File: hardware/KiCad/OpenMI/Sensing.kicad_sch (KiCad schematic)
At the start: 11 parts, among them U2 INA381A2IDGS

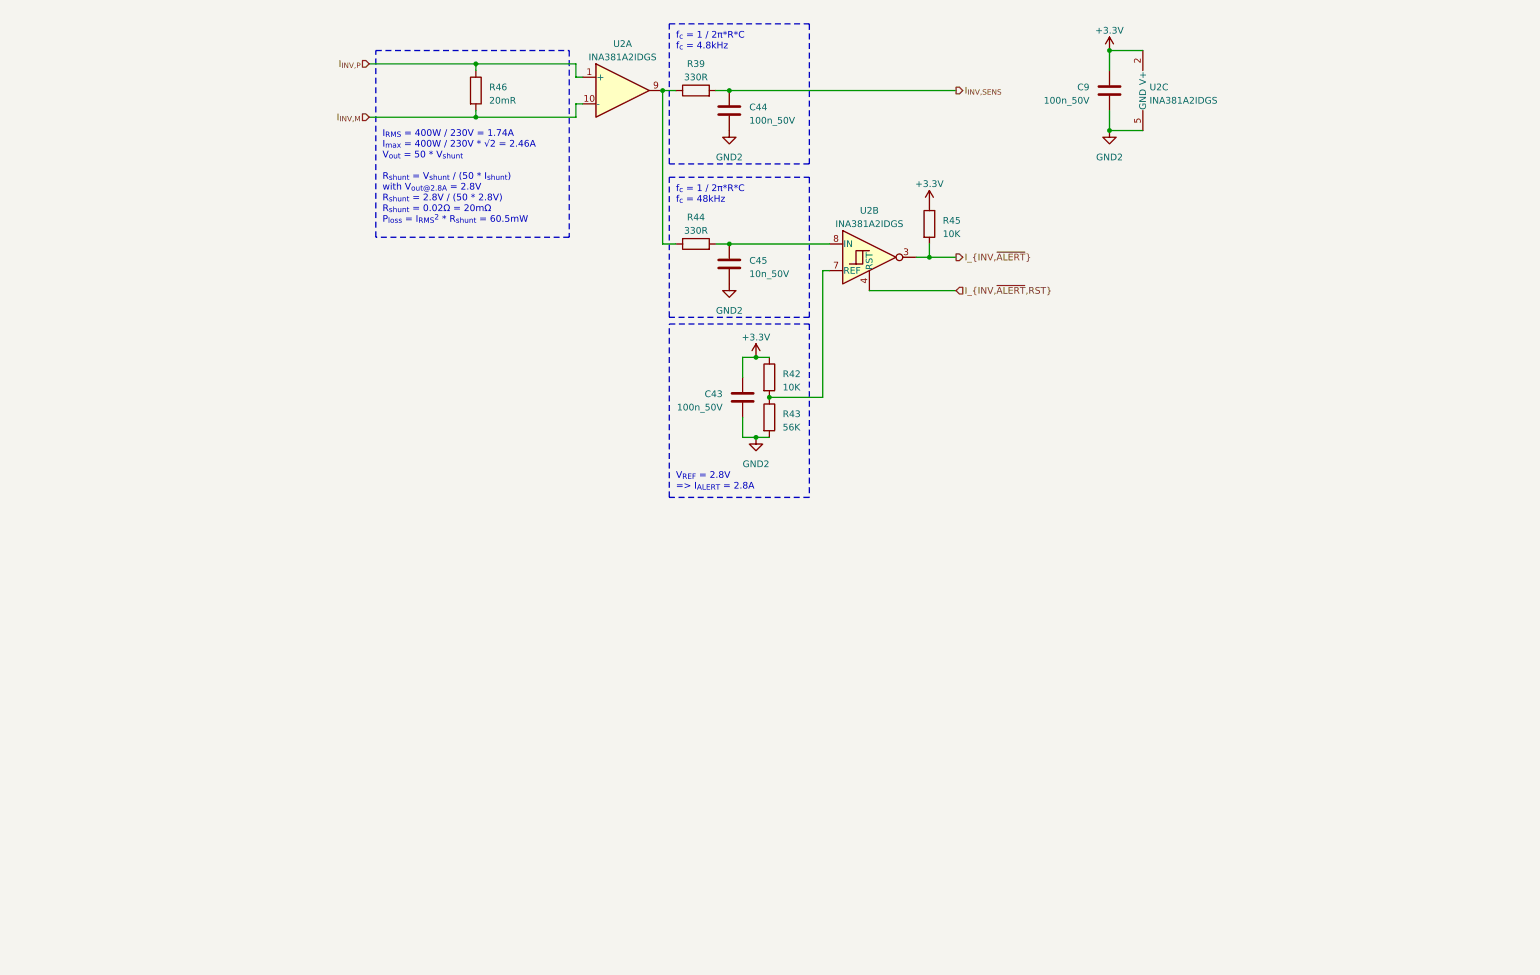
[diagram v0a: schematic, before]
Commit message: feat(hw): Moves DC-bus sense to Sensing sheet. Adds op-amp for impedance decoupling.
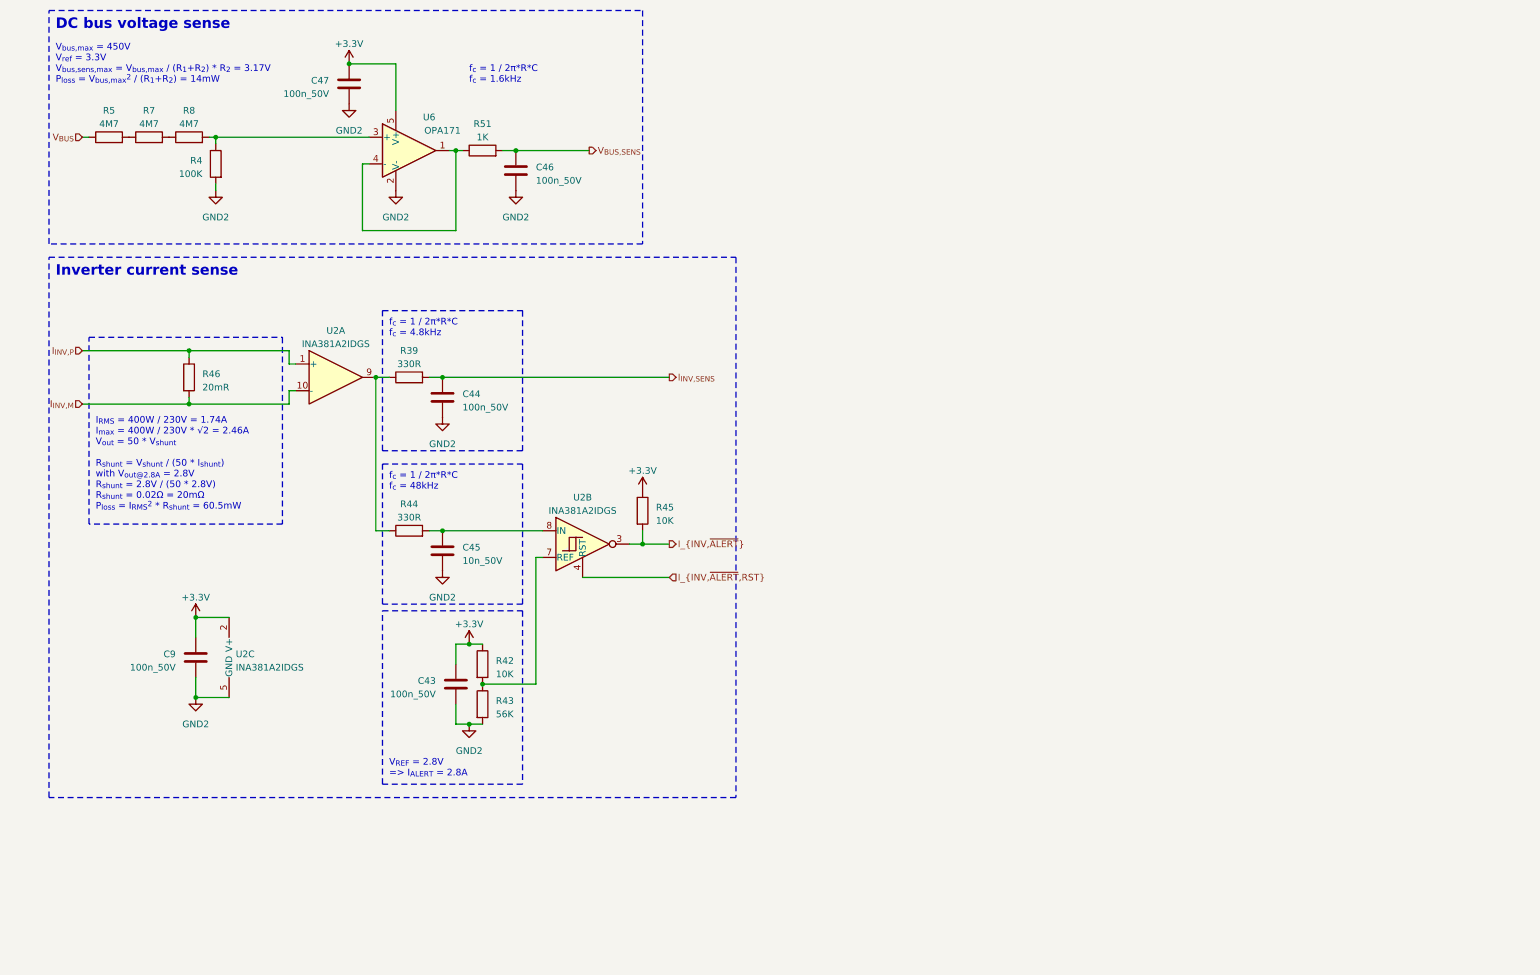
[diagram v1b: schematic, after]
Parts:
- added C46, C47: 100n_50V, Capacitor_SMD:C_0603_1608Metric, symbol _C_0603:100n_50V
- added R4: 100K, Resistor_SMD:R_0603_1608Metric, symbol _R_0603:100K
- added R5, R7, R8: 4M7, Resistor_SMD:R_1206_3216Metric, symbol _R_1206:4M7
- added R51: 1K, Resistor_SMD:R_0603_1608Metric, symbol _R_0603:1K
- added U6: OPA171, Package_TO_SOT_SMD:SOT-23-5, symbol _Amplifier_Operational:OPA171
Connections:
- net +3.3V: now also C47.1, U6.5 (V+)
- net GND2: now also C46.2, C47.2, R4.2, U6.2 (V-)
- new net: R7.2, R8.1
- new net: R4.1, R8.2, U6.3 (+)
- new net: R5.2, R7.1
- new net: R51.1, U6.1, U6.4 (-)
- new net V_{BUS,SENS}: C46.1, R51.2
- new net V_{BUS}: R5.1
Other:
- note added: "DC bus voltage sense"
- note added: "Inverter current sense"
- note added: "V_{bus,max} = 450V V_{ref} = 3.3V V_{bus,sens,max} = V_{bus,max} / (R_{1}+R_{2}) * R_{2} = 3.17V P_{loss} = V_{bus,max}^{2} / (R_{1}+R_{2}) = 14mW"
- note added: "f_{c} = 1 / 2π*R*C f_{c} = 1.6kHz"
- moved on the sheet: C43, C44, C45, C9, R39, R42, R43, R44, R45, R46, U2A, U2B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

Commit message: refactor(hw): Replaces OPA171 with pin compatible MCP6001T
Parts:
- removed U6: OPA171, Package_TO_SOT_SMD:SOT-23-5, symbol _Amplifier_Operational:OPA171
- added U7: MCP6001T-OT, Package_TO_SOT_SMD:SOT-23-5, symbol _Amplifier_Operational:MCP6001T-OT
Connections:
- net +3.3V: now also U7.5 (V+)
- net GND2: now also U7.2 (V-)
- net at R4.1, R8.2: now also U7.3 (+)
- net at R51.1: now also U7.1, U7.4 (-)
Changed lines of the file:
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@@
-    )
-  )
-  (symbol (lib_id "_Amplifier_Operational:OPA171") (at 82.55 40.64 0) (unit 1)
-    (in_bom yes) (on_board yes) (dnp no)
-    (property "Reference" "U6" (at 86.36 34.29 0)
-      (effects (font (size 1.27 1.27)))
-    )
-    (property "Value" "OPA171" (at 88.9 36.83 0)
-      (effects (font (size 1.27 1.27)))
-    )
-    (property "Footprint" "Package_TO_SOT_SMD:SOT-23-5" (at 82.55 40.64 0)
-      (effects (font (size 1.27 1.27)) hide)
-    )
-    (property "Datasheet" "http://www.ti.com/lit/ds/symlink/opa171.pdf" (at 82.55 35.56 0)
-      (effects (font (size 1.27 1.27)) hide)
-    )
-    (property "MF" "Texas Instruments" (at 82.55 40.64 0)
-      (effects (font (size 1.27 1.27)) hide)
-    )
-    (property "MPN" "OPA171AIDBV(R/T)" (at 82.55 40.64 0)
-      (effects (font (size 1.27 1.27)) hide)
-    )
-    (property "OC_CONRAD" "" (at 82.55 40.64 0)
-      (effects (font (size 1.27 1.27)) hide)
-    )
-    (property "OC_FARNELL" "" (at 82.55 40.64 0)
-      (effects (font (size 1.27 1.27)) hide)
-    )
-    (property "OC_LCSC" "" (at 82.55 40.64 0)
-      (effects (font (size 1.27 1.27)) hide)
-    )
-    (property "OC_MOUSER" "595-OPA171AIDBVR" (at 82.55 40.64 0)
-      (effects (font (size 1.27 1.27)) hide)
-    )
-    (property "OC_REICHELT" "" (at 82.55 40.64 0)
-      (effects (font (size 1.27 1.27)) hide)
-    )
-    (pin "2")
-    (pin "5")
-    (pin "1")
-    (pin "3")
-    (pin "4")
-    (instances
-      (project "OpenMI"
-        (path "/2d959e19-1572-42a0-a8fd-da8463ad4e66/bb3056b4-4e5d-4f2d-baa2-a568d9d3e754"
-          (reference "U6") (unit 1)
-        )
-      )
     )
   )
@@
         )
       )
+    )
+  )
+  (symbol (lib_id "_Amplifier_Operational:MCP6001T-OT") (at 82.55 40.64 0) (unit 1)
+    (in_bom yes) (on_board yes) (dnp no)
+    (property "Reference" "U7" (at 87.63 31.75 0)
+      (effects (font (size 1.27 1.27)))
+    )
+    (property "Value" "MCP6001T-OT" (at 87.63 34.29 0)
+      (effects (font (size 1.27 1.27)))
+    )
+    (property "Footprint" "Package_TO_SOT_SMD:SOT-23-5" (at 80.01 45.72 0)
+      (effects (font (size 1.27 1.27)) (justify left) hide)
+    )
+    (property "Datasheet" "http://ww1.microchip.com/downloads/en/DeviceDoc/MCP6001-1R-1U-2-4-1-MHz-Low-Power-Op-Amp-DS20001733L.pdf" (at 82.55 40.64 0)
+      (effects (font (size 1.27 1.27)) hide)
+    )
+    (property "MF" "Microchip Technology" (at 82.55 40.64 0)
+      (effects (font (size 1.27 1.27)) hide)
+    )
+    (property "MPN" "MCP6001T-I/OT" (at 82.55 40.64 0)
+      (effects (font (size 1.27 1.27)) hide)
+    )
+    (property "OC_CONRAD" "" (at 82.55 40.64 0)
+      (effects (font (size 1.27 1.27)) hide)
+    )
+    (property "OC_FARNELL" "" (at 82.55 40.64 0)
+      (effects (font (size 1.27 1.27)) hide)
+    )
+    (property "OC_LCSC" "C116490" (at 82.55 40.64 0)
+      (effects (font (size 1.27 1.27)) hide)
+    )
+    (property "OC_MOUSER" "579-MCP6001T-I/OT" (at 82.55 40.64 0)
+      (effects (font (size 1.27 1.27)) hide)
+    )
+    (property "OC_REICHELT" "" (at 82.55 40.64 0)
+      (effects (font (size 1.27 1.27)) hide)
+    )
+    (pin "2")
+    (pin "5")
+    (pin "1")
+    (pin "3")
+    (pin "4")
+    (instances
+      (project "OpenMI"
+        (path "/2d959e19-1572-42a0-a8fd-da8463ad4e66/bb3056b4-4e5d-4f2d-baa2-a568d9d3e754"
+          (reference "U7") (unit 1)
+        )
+      )

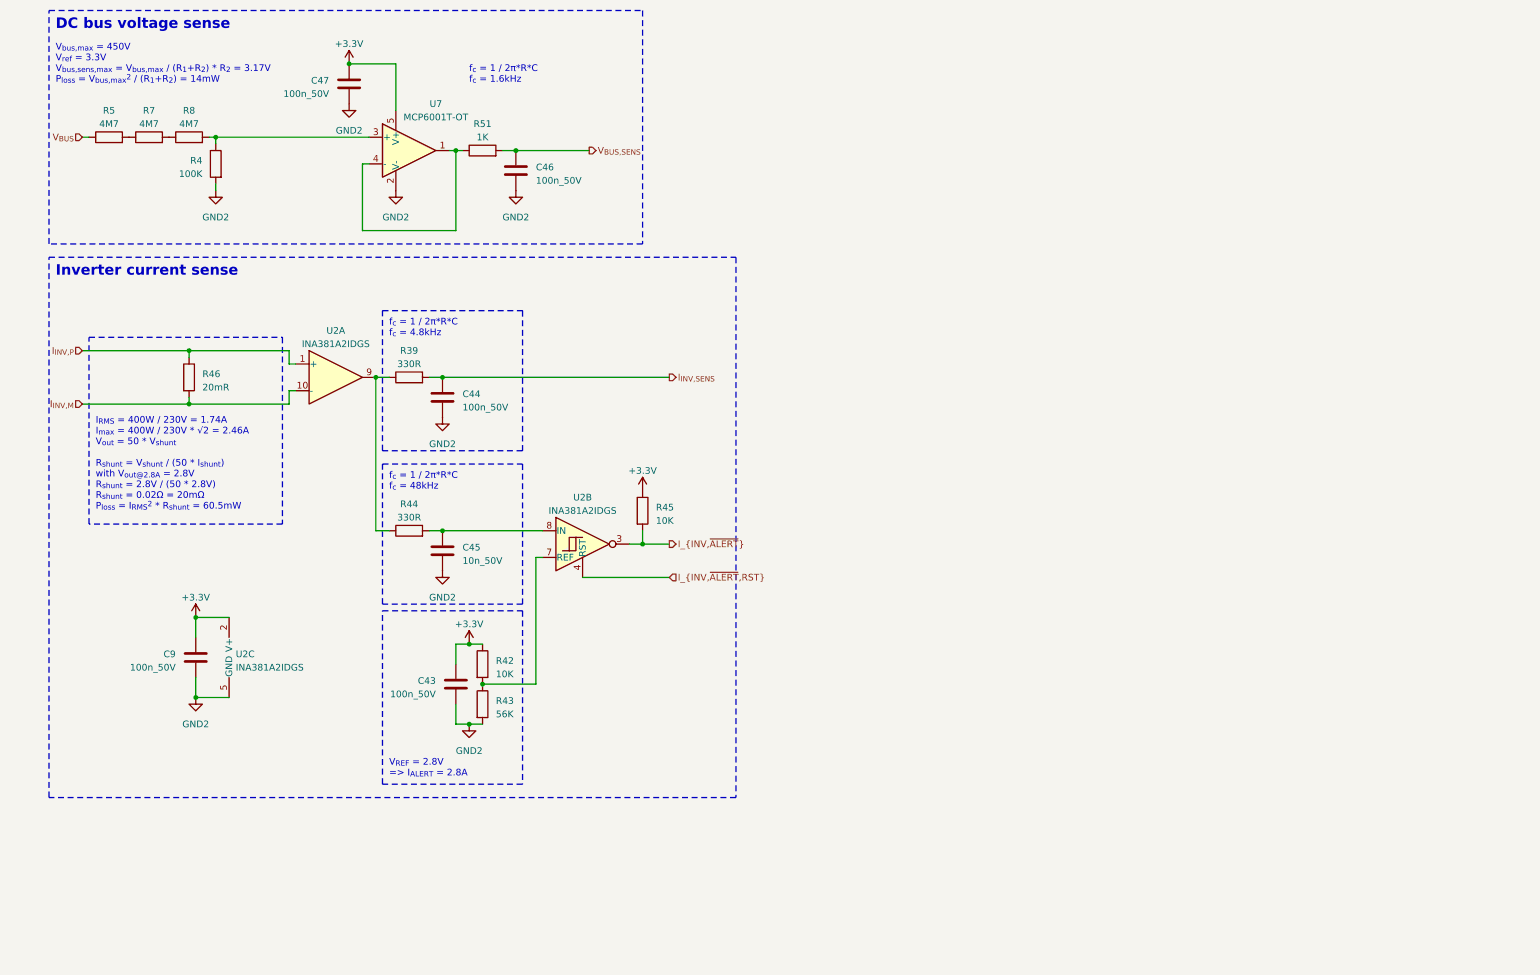
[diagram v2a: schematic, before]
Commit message: refactor(hw): Moves grid voltage sensing to `Sensing`. Refactors labels.
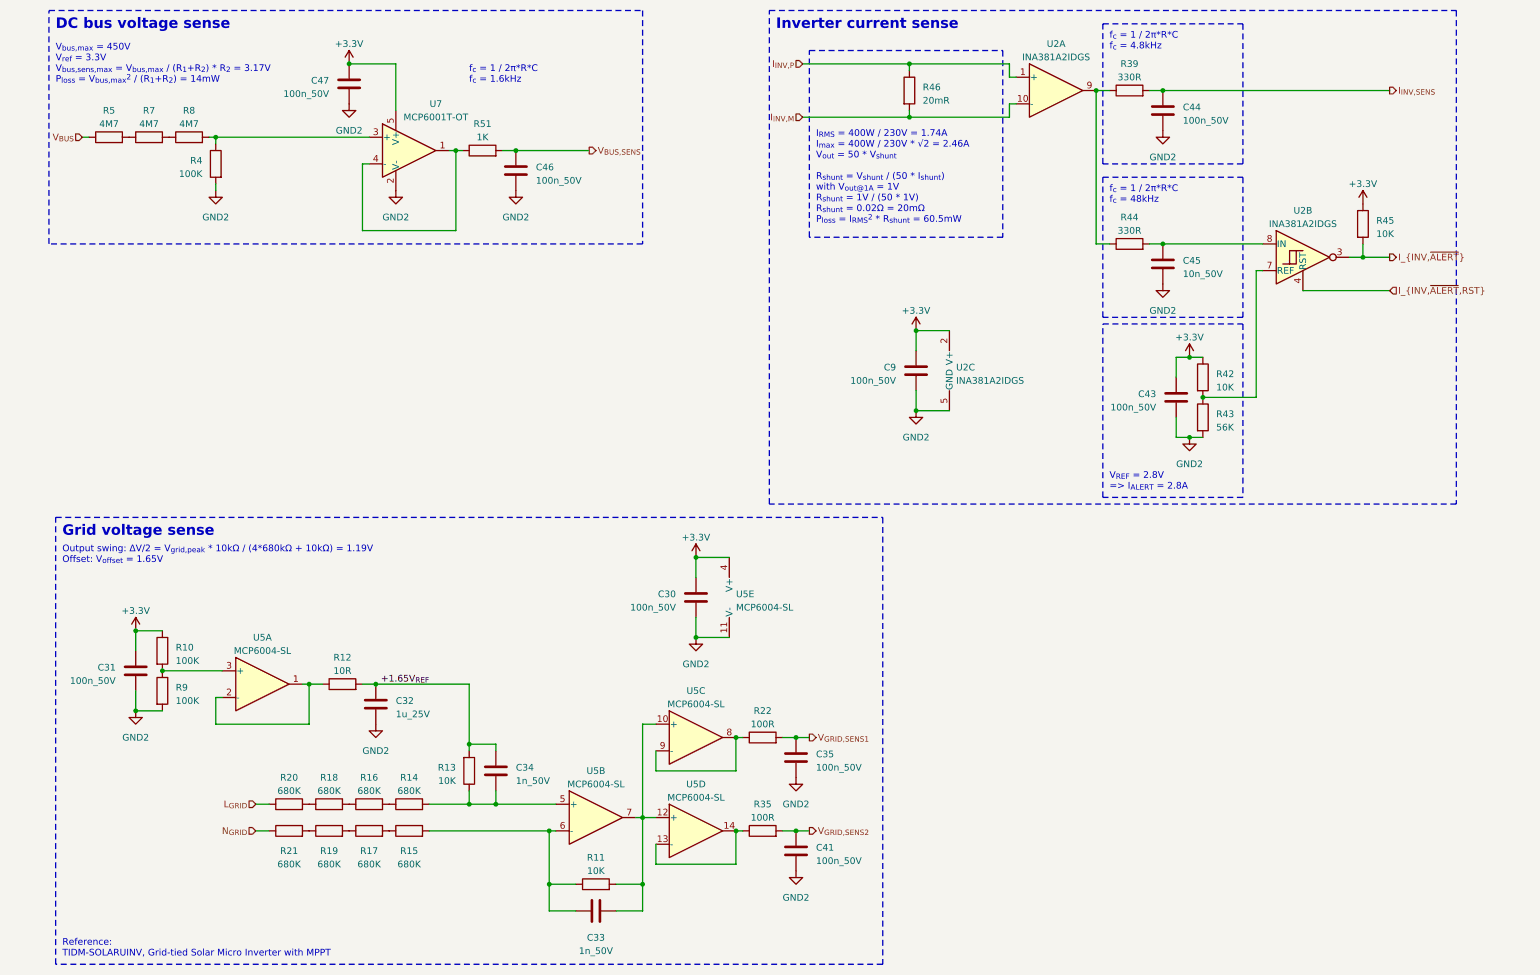
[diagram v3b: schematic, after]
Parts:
- added C30, C31, C35, C41: 100n_50V, Capacitor_SMD:C_0603_1608Metric, symbol _C_0603:100n_50V
- added C32: 1u_25V, Capacitor_SMD:C_0805_2012Metric, symbol _C_0805:1u_25V
- added C33, C34: 1n_50V, Capacitor_SMD:C_0603_1608Metric, symbol _C_0603:1n_50V
- added R10, R9: 100K, Resistor_SMD:R_0603_1608Metric, symbol _R_0603:100K
- added R11, R13: 10K, Resistor_SMD:R_0603_1608Metric, symbol _R_0603:10K
- added R12: 10R, Resistor_SMD:R_0603_1608Metric, symbol _R_0603:10R
- added R14, R15, R16, R17, R18, R19, R20, R21: 680K, Resistor_SMD:R_1206_3216Metric, symbol _R_1206:680K
- added R22, R35: 100R, Resistor_SMD:R_0603_1608Metric, symbol _R_0603:100R
- added U5: MCP6004-SL, Package_SO:SOIC-14_3.9x8.7mm_P1.27mm, symbol _Amplifier_Operational:MCP6004-SL
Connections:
- net +3.3V: now also C30.1, C31.1, R10.1, U5.4 (V+)
- net GND2: now also C30.2, C31.2, C32.2, C35.2, C41.2, R9.2, U5.11 (V-)
- new net: R10.2, R9.1, U5.3 (+)
- new net: R18.1, R20.2
- new net: R16.1, R18.2
- new net: C34.1, R13.1, R14.2, U5.5 (+)
- new net: C33.1, R11.1, R15.2, U5.6 (-)
- new net: C33.2, R11.2, U5.10 (+), U5.12 (+), U5.7
- new net: R12.1, U5.1, U5.2 (-)
- new net: R22.1, U5.8, U5.9 (-)
- new net: R35.1, U5.13 (-), U5.14
- new net: R14.1, R16.2
- new net: R19.1, R21.2
- new net: R17.1, R19.2
- new net: R15.1, R17.2
- new net +1.65V_{REF}: C32.1, C34.2, R12.2, R13.2
- new net L_{GRID}: R20.1
- new net N_{GRID}: R21.1
- new net V_{GRID,SENS1}: C35.1, R22.2
- new net V_{GRID,SENS2}: C41.1, R35.2
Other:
- note added: "Grid voltage sense"
- note added: "I_{RMS} = 400W / 230V = 1.74A I_{max} = 400W / 230V * √2 = 2.46A V_{out} = 50 * V_{shunt} R_{shunt} = V_{shunt} / (50 * I_{shunt}) with V_{out@1A} = 1V R_{shunt} = 1V / (50 * 1V) R_{shunt} = 0.02Ω = 20mΩ P_{loss} = I_{RMS}^{2} * R_{shunt} = 60.5mW"
- note added: "Output swing: ΔV/2 = V_{grid,peak} * 10kΩ / (4*680kΩ + 10kΩ) = 1.19V Offset: V_{offset} = 1.65V"
- note added: "Reference: TIDM-SOLARUINV, Grid-tied Solar Micro Inverter with MPPT"
- note removed: "I_{RMS} = 400W / 230V = 1.74A I_{max} = 400W / 230V * √2 = 2.46A V_{out} = 50 * V_{shunt} R_{shunt} = V_{shunt} / (50 * I_{shunt}) with V_{out@2.8A} = 2.8V R_{shunt} = 2.8V / (50 * 2.8V) R_{shunt} = 0.02Ω = 20mΩ P_{loss} = I_{RMS}^{2} * R_{shunt} = 60.5mW"
- moved on the sheet: C43, C44, C45, C9, R39, R42, R43, R44, R45, R46, U2A, U2B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
